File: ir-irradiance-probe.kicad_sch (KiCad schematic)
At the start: 56 parts, among them J1 USB-C_UJC-HP-3-SMT-TR, J2 SM04B-SRSS-TB-LF-SN, J3 PinHeader_1x2_P2.54mm_Drill1.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, J4 Conn_BNC_031-70526-21, SW1 MSS3-V-T_R, U1 TLV70033_SC70, U2 AD8604ARUZ, U3 ADC101C027CIMK

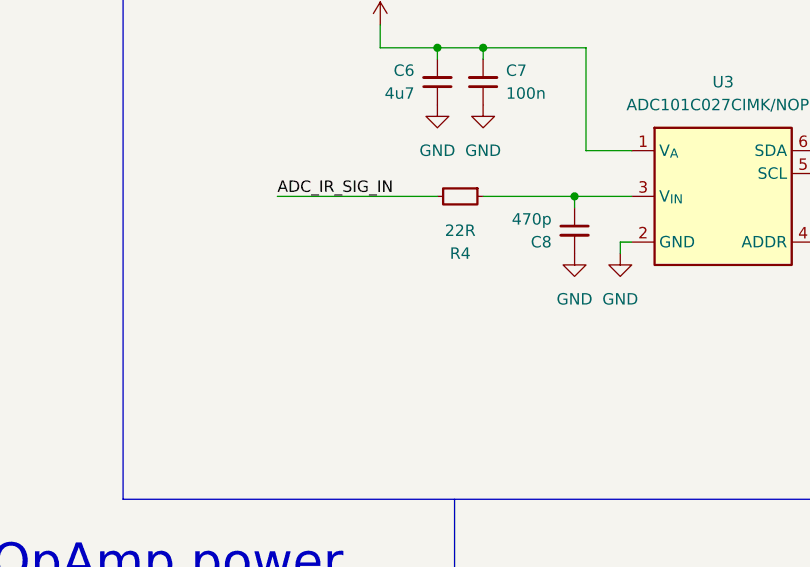
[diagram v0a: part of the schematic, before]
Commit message: [#47284] Updated RC filter on ADC input line
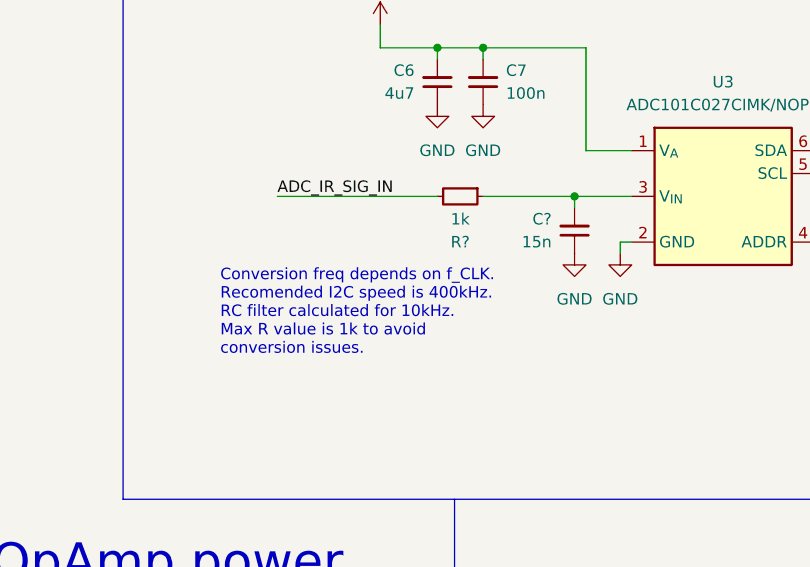
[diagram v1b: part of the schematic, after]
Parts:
- removed C8: C_470p_0402, ir-irradiance-probe-footprints:C_0402_1005Metric, symbol ir-irradiance-probe:C_470p_0402
- removed R4: R_22R_0402, ir-irradiance-probe-footprints:R_0402_1005Metric, symbol ir-irradiance-probe:R_22R_0402
- added C?: C_15n_0402, antmicro-footprints:C_0402_1005Metric, symbol antmicroCapacitors0402:C_15n_0402
- added R?: R_1k_0402, antmicro-footprints:R_0402_1005Metric, symbol antmicroResistors0402:R_1k_0402
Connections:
- net ADC_IR_SIG_IN: now also R?.2
- net GND: now also C?.1
- net at U3.3 (V_{IN}): now also C?.2, R?.1
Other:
- note added: "Conversion freq depends on f_CLK. Recomended I2C speed is 400kHz. RC filter calculated for 10kHz. Max R value is 1k to avoid conversion issues."

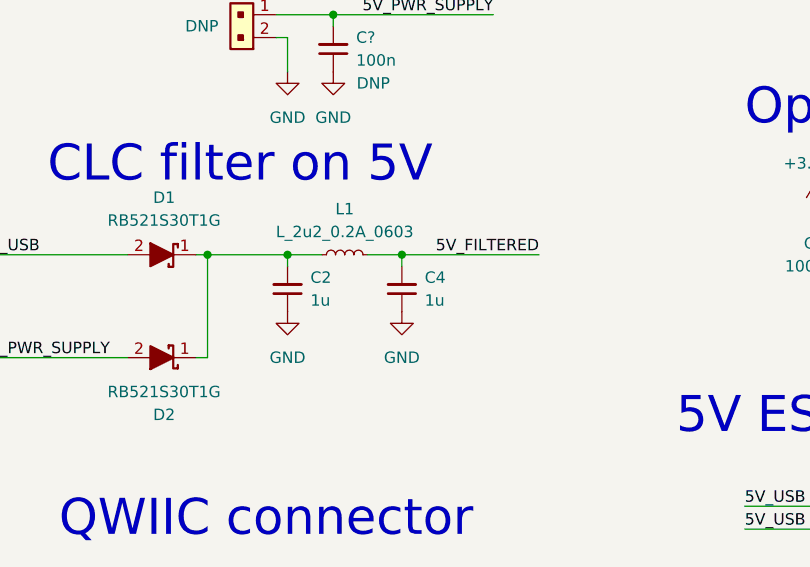
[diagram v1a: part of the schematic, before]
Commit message: [#47284] Updated CLC filter on 5V line
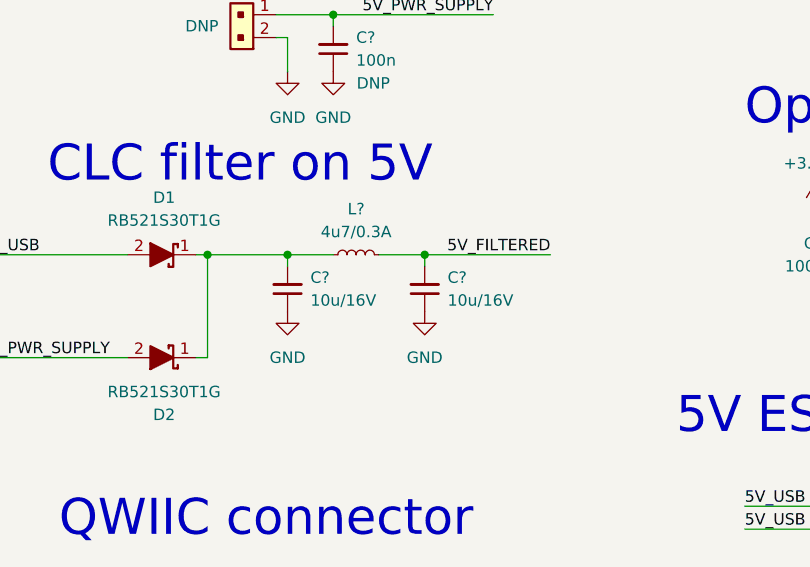
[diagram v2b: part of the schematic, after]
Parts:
- removed C2, C4: C_1u_0402, ir-irradiance-probe-footprints:C_0402_1005Metric, symbol ir-irradiance-probe:C_1u_0402
- removed L1: L_2u2_0.2A_0603, ir-irradiance-probe-footprints:L_0603_1608Metric, symbol ir-irradiance-probe:L_2u2_0.2A_0603
- added C? (x2): C_10u_16V_0603, antmicro-footprints:C_0603_1608Metric, symbol antmicroCapacitors0603:C_10u_16V_0603
- added L?: L_4u7_0.3A_0805, antmicro-footprints:L_0805_2012Metric, symbol antmicroFixedInductors:L_4u7_0.3A_0805
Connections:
- net 5V_FILTERED: now also C?.2, L?.2
- net GND: now also C?.1, C?.1
- net at D1.1, D2.1: now also C?.2, L?.1

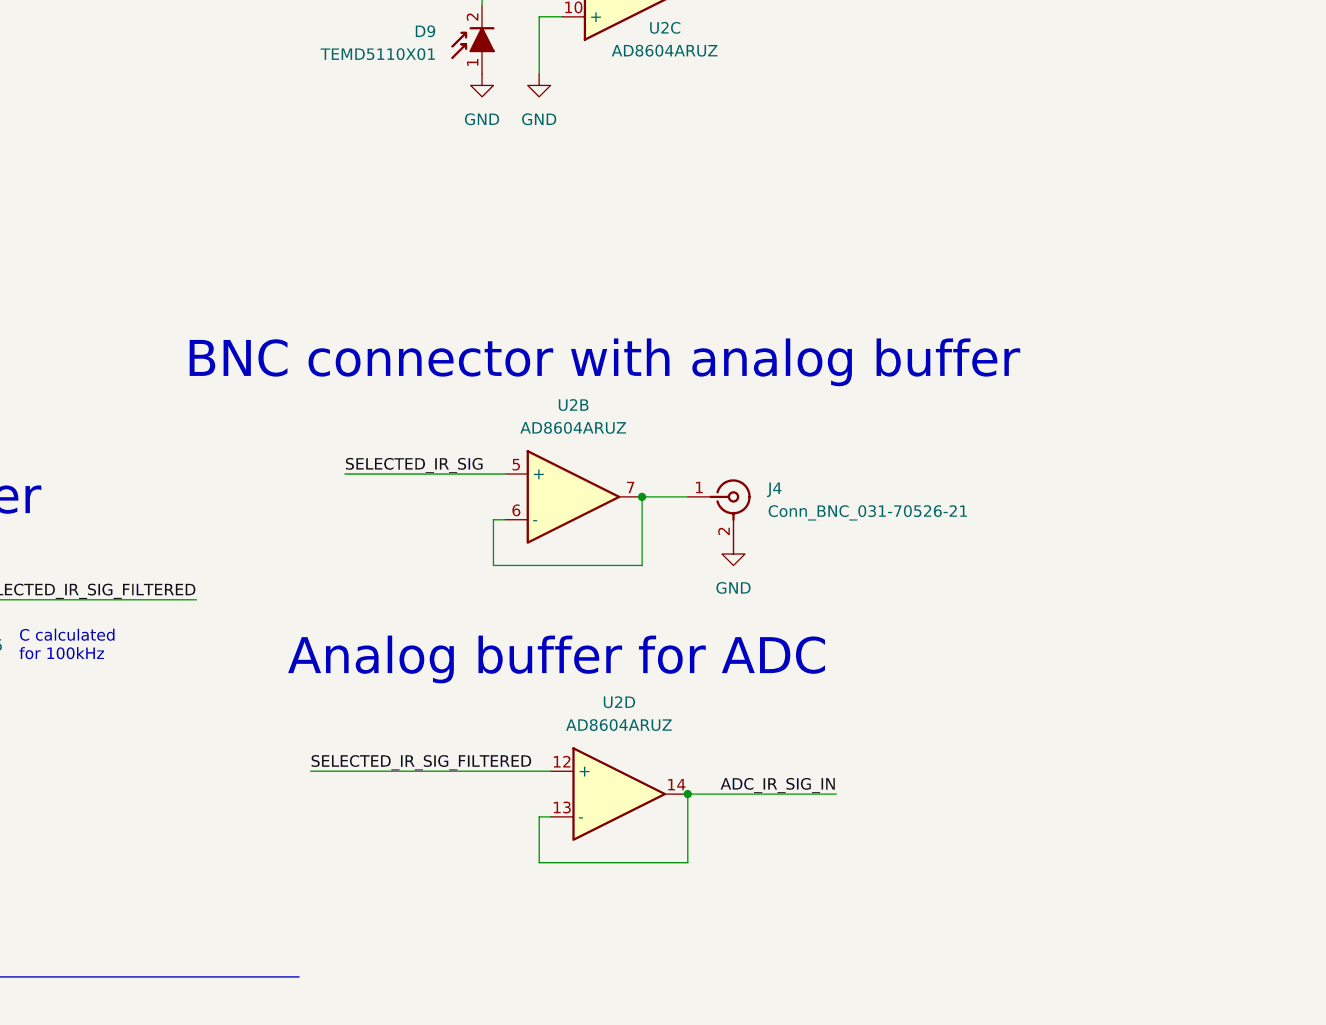
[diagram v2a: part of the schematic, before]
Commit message: [#47284] Add ESD protection on BNC connector
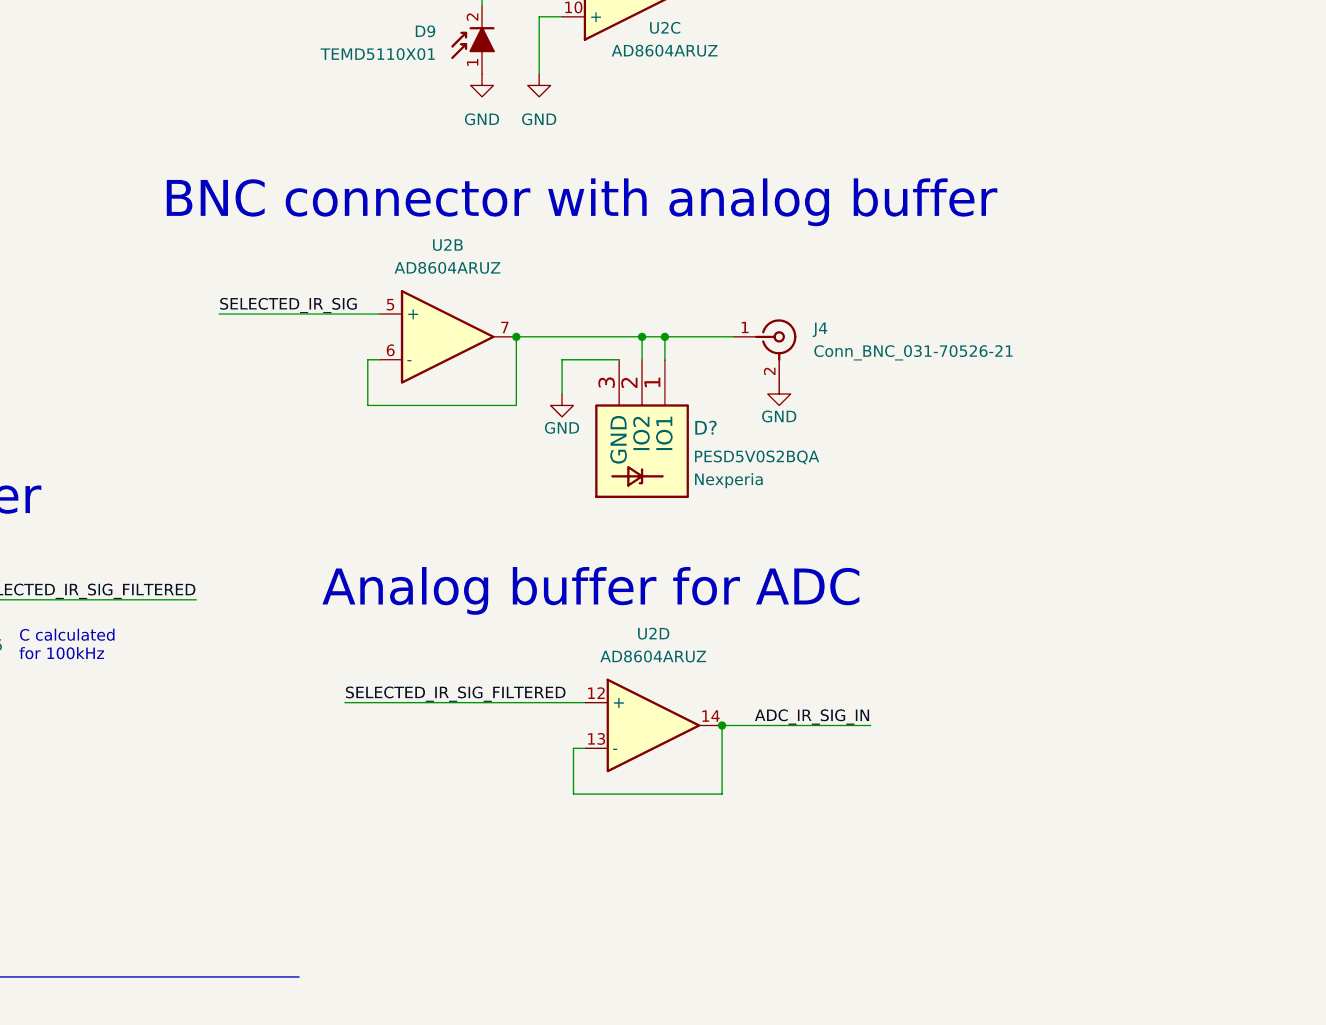
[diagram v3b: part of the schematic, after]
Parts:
- added D?: PESD5V0S2BQA, ir-irradiance-probe-footprints:TPD2E009DRTR, symbol ir-irradiance-probe:PESD5V0S2BQA
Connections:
- net GND: now also D?.3 (GND)
- net at J4.1, U2.6 (-), U2.7: now also D?.1 (IO1), D?.2 (IO2)
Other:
- moved on the sheet: J4, U2B, U2D

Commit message: [#47284] Annotated components and reorganised schematic
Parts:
- gave numbers to parts that had none: 10
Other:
- note removed: "Analog Section"
- note removed: "Digital Section"
- note removed: "Power Section"
- moved on the sheet: C1, C10, C11, C12, C13, C14, C2, C3, C4, C5, C6, C7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

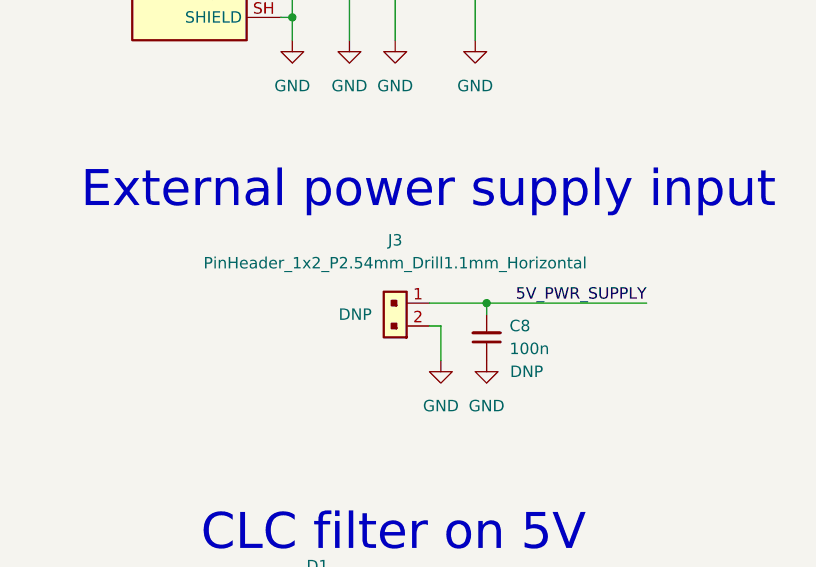
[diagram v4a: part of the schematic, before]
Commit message: [#47284] Updated PCB layout
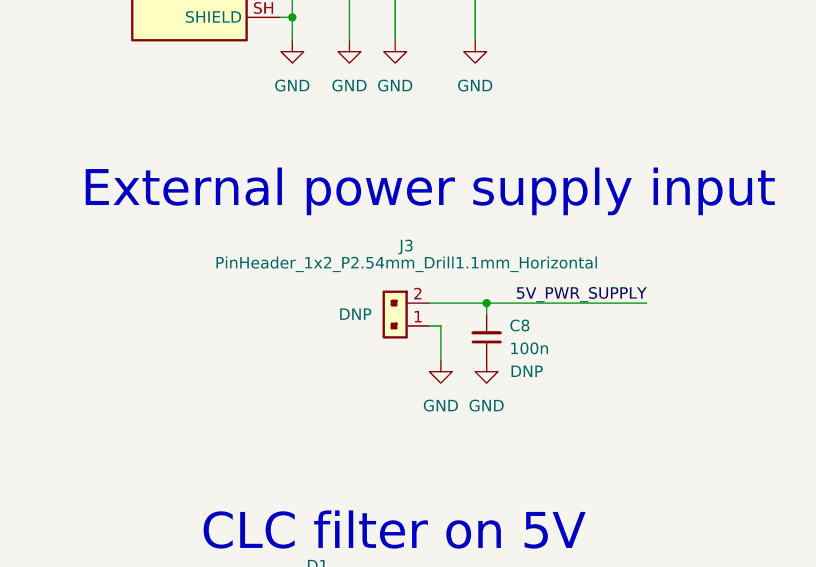
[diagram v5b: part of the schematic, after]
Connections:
- net 5V_PWR_SUPPLY: now also J3.2; no longer J3.1
- net GND: now also J3.1; no longer J3.2
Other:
- moved on the sheet: J3
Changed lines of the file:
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@@
     (pin "2")
   )
-  (symbol (lib_id "ir-irradiance-probe:PinHeader_1x2_P2.54mm_Drill1.1mm_Horizontal") (at 57.15 92.71 0) (mirror y) (unit 1)
+  (symbol (lib_id "ir-irradiance-probe:PinHeader_1x2_P2.54mm_Drill1.1mm_Horizontal") (at 57.15 95.25 180) (unit 1)
     (in_bom yes) (on_board yes)
-    (property "Reference" "J3" (id 0) (at 53.34 85.725 0)
+    (property "Reference" "J3" (id 0) (at 54.61 86.36 0)
       (effects (font (size 1.27 1.27) (thickness 0.15)))
     )
-    (property "Value" "PinHeader_1x2_P2.54mm_Drill1.1mm_Horizontal" (id 1) (at 53.34 88.265 0)
+    (property "Value" "PinHeader_1x2_P2.54mm_Drill1.1mm_Horizontal" (id 1) (at 54.61 88.265 0)
       (effects (font (size 1.27 1.27) (thickness 0.15)))
     )
-    (property "Footprint" "ir-irradiance-probe-footprints:PinHeader_1x02_P2.54mm_Horizontal" (id 2) (at 36.83 102.87 0)
+    (property "Footprint" "ir-irradiance-probe-footprints:PinHeader_1x02_P2.54mm_Horizontal" (id 2) (at 36.83 85.09 0)
       (effects (font (size 1.27 1.27) (thickness 0.15)) (justify left bottom) hide)
     )
-    (property "Datasheet" "https://www.we-online.com/components/products/datasheet/61300211021.pdf" (id 3) (at 36.83 105.41 0)
+    (property "Datasheet" "https://www.we-online.com/components/products/datasheet/61300211021.pdf" (id 3) (at 36.83 82.55 0)
       (effects (font (size 1.27 1.27) (thickness 0.15)) (justify left bottom) hide)
     )
-    (property "MPN" "61300211021" (id 4) (at 36.83 107.95 0)
+    (property "MPN" "61300211021" (id 4) (at 36.83 80.01 0)
       (effects (font (size 1.27 1.27) (thickness 0.15)) (justify left bottom) hide)
     )
-    (property "Manufacturer" "Würth Elektronik" (id 5) (at 36.83 110.49 0)
+    (property "Manufacturer" "Würth Elektronik" (id 5) (at 36.83 77.47 0)
       (effects (font (size 1.27 1.27) (thickness 0.15)) (justify left bottom) hide)
     )
-    (property "Author" "Antmicro" (id 6) (at 36.83 113.03 0)
+    (property "Author" "Antmicro" (id 6) (at 36.83 74.93 0)
       (effects (font (size 1.27 1.27) (thickness 0.15)) (justify left bottom) hide)
     )
-    (property "License" "Apache-2.0" (id 7) (at 36.83 115.57 0)
+    (property "License" "Apache-2.0" (id 7) (at 36.83 72.39 0)
       (effects (font (size 1.27 1.27) (thickness 0.15)) (justify left bottom) hide)
     )

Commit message: [#47284] Run kmake loclib
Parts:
- C12, C2, C8: footprint antmicro-footprints:C_0402_1005Metric -> ir-irradiance-probe-footprints:C_0402_1005Metric; symbol antmicroCapacitors0402:C_100n_0402 -> ir-irradiance-probe:C_100n_0402
- C13, C4: footprint antmicro-footprints:C_0603_1608Metric -> ir-irradiance-probe-footprints:C_0603_1608Metric; symbol antmicroCapacitors0603:C_10u_16V_0603 -> ir-irradiance-probe:C_10u_16V_0603
- C14: footprint antmicro-footprints:C_0402_1005Metric -> ir-irradiance-probe-footprints:C_0402_1005Metric; symbol antmicroCapacitors0402:C_15n_0402 -> ir-irradiance-probe:C_15n_0402
- D9: footprint antmicro-footprints:Photodiode_SMD_4.2x5mm_TEMD -> ir-irradiance-probe-footprints:Photodiode_SMD_4.2x5mm_TEMD; symbol antmicroOpticalSensorsReflectiveAnalogOutput:TEMD5110X01 -> ir-irradiance-probe:TEMD5110X01
- L1: footprint antmicro-footprints:L_0805_2012Metric -> ir-irradiance-probe-footprints:L_0805_2012Metric; symbol antmicroFixedInductors:L_4u7_0.3A_0805 -> ir-irradiance-probe:L_4u7_0.3A_0805
- R4: footprint antmicro-footprints:R_0402_1005Metric -> ir-irradiance-probe-footprints:R_0402_1005Metric; symbol antmicroResistors0402:R_1k_0402 -> ir-irradiance-probe:R_1k_0402
